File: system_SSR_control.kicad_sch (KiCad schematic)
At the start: 13 parts, among them J1 171857-0003, Q1 2.1V, Q2 2N7000, Q3 2N7000, SW1 FSM2JSMA, SW2 FSM2JSMA

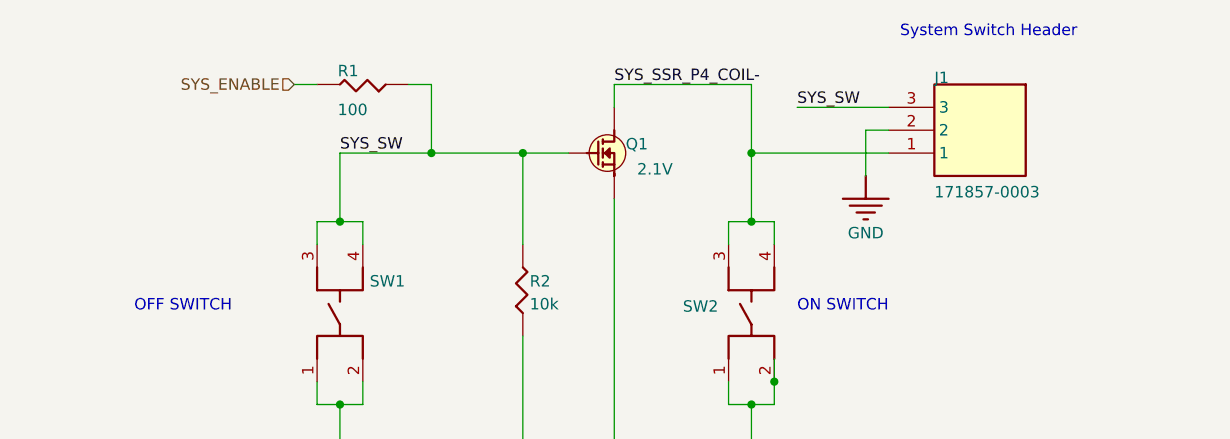
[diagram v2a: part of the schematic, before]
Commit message: Finished updating all input and output headers
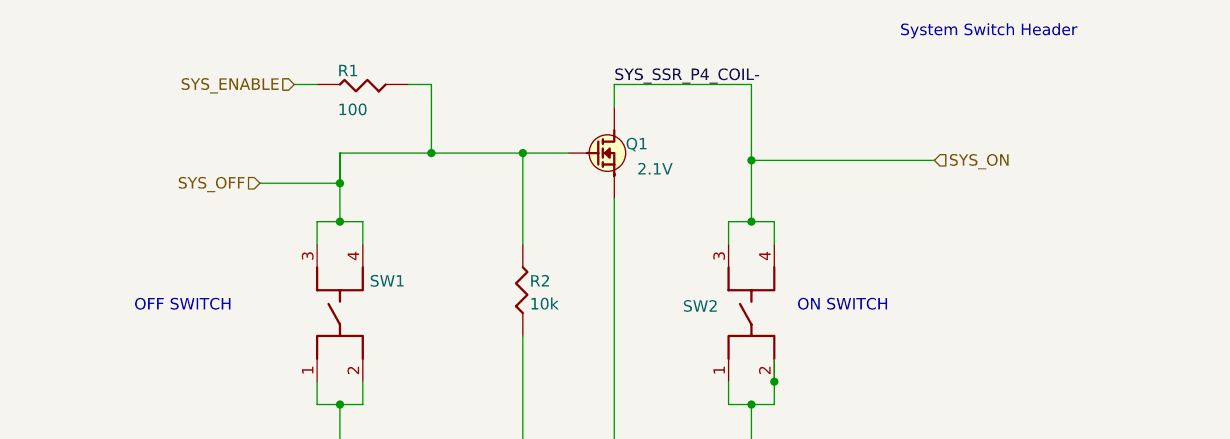
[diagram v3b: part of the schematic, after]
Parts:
- removed J1: 171857-0003, AltiumImport:171857-0003, symbol MEB-altium-import:system_SSR_control_0_171857-0003
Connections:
- net SYS_SSR_P4_COIL- renamed SYS_ON
- net SYS_SW renamed SYS_OFF
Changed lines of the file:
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@@
   (junction (at 195.58 154.1272) (diameter 0) (color 0 0 0 0)
   )
+  (junction (at 119.38 86.36) (diameter 0) (color 0 0 0 0)
+  )
   (junction (at 101.6 138.8872) (diameter 0) (color 0 0 0 0)
   )
@@
   (junction (at 101.6 161.7472) (diameter 0) (color 0 0 0 0)
   )
+  (junction (at 165.1 83.82) (diameter 0) (color 0 0 0 0)
+  )
   (junction (at 129.54 83.0072) (diameter 0) (color 0 0 0 0)
   )
@@
   (junction (at 111.76 161.7472) (diameter 0) (color 0 0 0 0)
   )
-  (junction (at 165.1 83.0072) (diameter 0) (color 0 0 0 0)
-  )
   (wire (pts (xy 200.66 167.64) (xy 195.58 167.64))
     (stroke (width 0.254) (type default))
   )
-  (wire (pts (xy 180.34 80.4672) (xy 177.8 80.4672))
-    (stroke (width 0.254) (type default))
-  )
   (wire (pts (xy 111.76 138.8872) (xy 111.76 141.4272))
     (stroke (width 0.254) (type default))
@@
     (stroke (width 0.254) (type default))
   )
-  (wire (pts (xy 119.38 83.0072) (xy 119.38 90.6272))
+  (wire (pts (xy 119.38 83.0072) (xy 119.38 86.36))
     (stroke (width 0.254) (type default))
   )
@@
     (stroke (width 0.254) (type default))
   )
+  (wire (pts (xy 110.49 86.36) (xy 119.38 86.36))
+    (stroke (width 0) (type default))
+  )
   (wire (pts (xy 111.76 161.7472) (xy 119.38 161.7472))
     (stroke (width 0.254) (type default))
@@
     (stroke (width 0.254) (type default))
   )
-  (wire (pts (xy 177.8 80.4672) (xy 177.8 85.5472))
-    (stroke (width 0.254) (type default))
-  )
   (wire (pts (xy 222.25 160.02) (xy 198.12 160.02))
     (stroke (width 0.254) (type default))
@@
     (stroke (width 0.254) (type default))
   )
+  (wire (pts (xy 119.38 86.36) (xy 119.38 90.6272))
+    (stroke (width 0.254) (type default))
+  )
   (wire (pts (xy 167.64 105.8672) (xy 167.64 108.4072))
     (stroke (width 0.254) (type default))
@@
     (stroke (width 0.254) (type default))
   )
-  (wire (pts (xy 180.34 77.9272) (xy 170.18 77.9272))
-    (stroke (width 0.254) (type default))
-  )
   (wire (pts (xy 162.56 93.1672) (xy 162.56 90.6272))
     (stroke (width 0.254) (type default))
@@
     (stroke (width 0.254) (type default))
   )
-  (wire (pts (xy 165.1 90.6272) (xy 165.1 83.0072))
+  (wire (pts (xy 165.1 90.6272) (xy 165.1 83.82))
     (stroke (width 0.254) (type default))
   )
@@
     (stroke (width 0.254) (type default))
   )
-  (wire (pts (xy 165.1 83.0072) (xy 165.1 75.3872))
-    (stroke (width 0.254) (type default))
-  )
   (wire (pts (xy 167.64 90.6272) (xy 167.64 93.1672))
     (stroke (width 0.254) (type default))
@@
     (stroke (width 0.254) (type default))
   )
+  (wire (pts (xy 165.1 75.3872) (xy 165.1 83.82))
+    (stroke (width 0.254) (type default))
+  )
+  (wire (pts (xy 119.38 83.0072) (xy 119.38 86.36))
+    (stroke (width 0) (type default))
+  )
   (wire (pts (xy 137.16 161.7472) (xy 134.62 161.7472))
     (stroke (width 0.254) (type default))
@@
     (stroke (width 0.254) (type default))
   )
-  (wire (pts (xy 165.1 83.0072) (xy 180.34 83.0072))
+  (wire (pts (xy 165.1 83.82) (xy 185.42 83.82))
     (stroke (width 0.254) (type default))
   )
@@
     (effects (font (size 1.27 1.27)) (justify left bottom))
   )
-  (label "SYS_SW" (at 119.38 83.0072 0) (fields_autoplaced)
-    (effects (font (size 1.27 1.27)) (justify left bottom))
-  )
   (label "SYS_SSR_P4_COIL-" (at 149.86 75.3872 0) (fields_autoplaced)
     (effects (font (size 1.27 1.27)) (justify left bottom))
@@
     (effects (font (size 1.27 1.27)) (justify left bottom))
   )
-  (label "SYS_SW" (at 170.18 77.9272 0) (fields_autoplaced)
-    (effects (font (size 1.27 1.27)) (justify left bottom))
+  (hierarchical_label "SYS_ON" (shape input) (at 185.42 83.82 0) (fields_autoplaced)
+    (effects (font (size 1.27 1.27)) (justify left))
   )
   (hierarchical_label "KillSwitchA" (shape input) (at 200.66 167.64 0) (fields_autoplaced)
@@
   )
   (hierarchical_label "THR_KILLED" (shape output) (at 86.36 161.7472 180) (fields_autoplaced)
+    (effects (font (size 1.27 1.27)) (justify right))
+  )
+  (hierarchical_label "SYS_OFF" (shape input) (at 110.49 86.36 180) (fields_autoplaced)
     (effects (font (size 1.27 1.27)) (justify right))
   )
@@
     )
   )
-  (symbol (lib_id "MEB-altium-import:GND") (at 177.8 85.5472 0) (unit 1)
-    (in_bom yes) (on_board yes) (dnp no)
-    (property "Reference" "#PWR0121" (at 177.8 85.5472 0)
-      (effects (font (size 1.27 1.27)) hide)
-    )
-    (property "Value" "GND" (at 177.8 91.8972 0)
-      (effects (font (size 1.27 1.27)))
-    )
-    (property "Footprint" "" (at 177.8 85.5472 0)
-      (effects (font (size 1.27 1.27)) hide)
-    )
-    (property "Datasheet" "" (at 177.8 85.5472 0)
-      (effects (font (size 1.27 1.27)) hide)
-    )
-    (pin "")
-    (instances
-      (project "MEB"
-        (path "/228e4997-23c1-4c21-939b-583cad26a5e3/d2748488-1aa2-4890-bfa9-60c09f864312"
-          (reference "#PWR0121") (unit 1)
-        )
-      )
-    )
-  )
   (symbol (lib_id "MEB-altium-import:system_SSR_control_0_N-MOSFET") (at 149.86 83.0072 0) (unit 1)
     (in_bom yes) (on_board yes) (dnp no)
@@
         )
       )
-    )
-  )
-  (symbol (lib_id "MEB-altium-import:system_SSR_control_0_171857-0003") (at 180.34 77.9272 0) (unit 1)
-    (in_bom yes) (on_board yes) (dnp no)
-    (property "Reference" "J1" (at 185.42 75.3872 0)
-      (effects (font (size 1.27 1.27)) (justify left bottom))
-    )
-    (property "Value" "171857-0003" (at 185.42 88.0872 0)
-      (effects (font (size 1.27 1.27)) (justify left bottom))
-    )
-    (property "Footprint" "AltiumImport:171857-0003" (at 180.34 77.9272 0)
-      (effects (font (size 1.27 1.27)) hide)
-    )
-    (property "Datasheet" "" (at 180.34 77.9272 0)
-      (effects (font (size 1.27 1.27)) hide)
-    )
-    (property "Part Number" "171857-0003" (at 180.34 77.9272 0)
-      (effects (font (size 1.27 1.27)) hide)
-    )
-    (pin "1")
-    (pin "2")
-    (pin "3")
-    (instances
-      (project "MEB"
-        (path "/228e4997-23c1-4c21-939b-583cad26a5e3/d2748488-1aa2-4890-bfa9-60c09f864312"
-          (reference "J1") (unit 1)
-        )
-      )

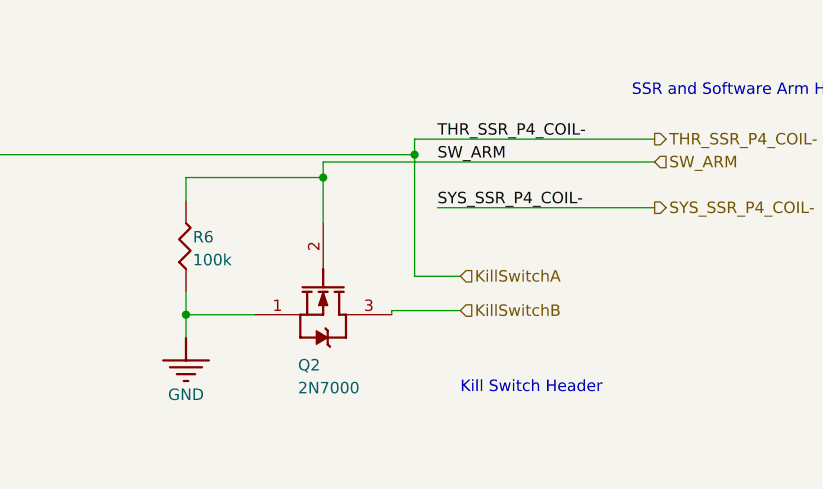
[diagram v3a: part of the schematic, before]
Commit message: Finalized schematic and began assigning footprints
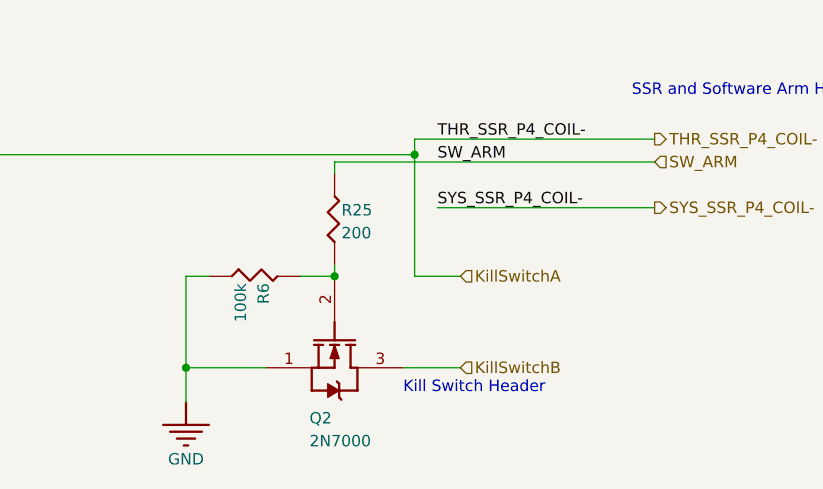
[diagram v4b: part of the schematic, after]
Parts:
- added R25: 200, Resistor_SMD:R_0805_2012Metric_Pad1.20x1.40mm_HandSolder, symbol MEB-altium-import:system_SSR_control_1_ERJ-6ENF1003V
- R1, R2, R3, R4, R5, R6: footprint AltiumImport:SMD-0805-RES -> Resistor_SMD:R_0805_2012Metric_Pad1.20x1.40mm_HandSolder
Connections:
- net SW_ARM: now also R25.2; no longer Q2.2 (G), R6.2
- new net: Q2.2 (G), R25.1, R6.2
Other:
- moved on the sheet: Q2, R6
